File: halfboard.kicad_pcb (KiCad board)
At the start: 2 copper layers, 117.4 x 87.9 mm, 54 parts, among them U1 

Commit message: move battery/switch and correct polarity
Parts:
- removed the   at (52.6, 48.5)
- removed REF**: SW_SPDT_PCM12, Button_Switch_SMD:SW_SPDT_PCM12
- added  : , Button_Switch_SMD:SW_SPDT_PCM12, F.Cu at (135.4, 130.6)
- added  : , Button_Switch_SMD:SW_SPDT_PCM12, B.Cu at (135.4, 130.6)
-  : renamed from REF**
-  : renamed from REF**; value SW_SPST_B3U-3000P-B -> (none)
- moved   60.5 mm to (80.0, 109.2)
- moved   33.0 mm to (48.8, 47.5) (x2)
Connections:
-   pad 1: row0 -> (no net) (x6)
-   pad 2: col5_row0 -> (no net)
-   pad 2: col4_row0 -> (no net)
-   pad 2: col3_row0 -> (no net)
-   pad 1: row1 -> (no net) (x6)
-   pad 2: col3_row1 -> (no net)
-   pad 1: row2 -> (no net) (x6)
-   pad 2: col3_row2 -> (no net)
-   pad 2: col2_row2 -> (no net)
-   pad 2: col2_row1 -> (no net)
-   pad 2: col1_row2 -> (no net)
-   pad 1: row3 -> (no net) (x6)
-   pad 2: col1_row3 -> (no net)
-   pad 2: col0_row3 -> (no net)
-   pad 2: col0_row2 -> (no net)
-   pad 2: col5_row1 -> (no net)
-   pad 2: col2_row0 -> (no net)
-   pad 2: col1_row0 -> (no net)
-   pad 2: col1_row1 -> (no net)
-   pad 2: col0_row1 -> (no net)
-   pad 2: col0_row0 -> (no net)
-   pad 2: col5_row2 -> (no net)
-   pad 2: col5_row3 -> (no net)
-   pad 1: BAT0 -> BAT_SW
-   pad 2: BAT_SW -> BAT0
-   pad 2: col4_row3 -> (no net)
-   pad 2: col3_row3 -> (no net)
-   pad 2: col2_row3 -> (no net)
-   pad 2: col4_row2 -> (no net)
-   pad 2: col4_row1 -> (no net)
- U1 pad 10: col1 -> (no net)
- U1 pad 12: col3 -> col1
- U1 pad 14: col5 -> (no net)
- U1 pad 15: (no net) -> col3
- U1 pad 16: (no net) -> col5
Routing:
- net BAT_GND: track 34.4 -> 150.2 mm
- net BAT0: track 5.98 -> 60.3 mm
- net col3: track 135.2 -> 90.8 mm, vias 0 -> 1
- net BAT_SW: track 33.2 -> 74.8 mm, vias 0 -> 1
- net row2: track 165.4 -> 132.4 mm, vias 1 -> 3
- net col2: track 153.6 -> 127.7 mm, vias 0 -> 3
- net col5: track 166.3 -> 140.7 mm
- net RESET: track 13.9 -> 33.0 mm
- net col4: track 150.3 -> 131.8 mm
- net row3: track 175.1 -> 158.3 mm, vias 0 -> 2
- net row1: track 117.9 -> 131.1 mm, vias 0 -> 2
- net col1: track 78.4 -> 66.7 mm
- net col0: track 90.5 -> 80.0 mm
- net (no net): track 5.70 -> 0.00 mm
- net col0_row1: track 22.1 -> 17.0 mm
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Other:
- outline, holes or cut-outs redrawn

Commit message: remove front silkscreens
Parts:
- removed the   at (135.4, 130.6) (x2)
- added  : , Button_Switch_SMD:SW_SPDT_PCM12, F.Cu at (135.4, 130.6)
- added  : , Button_Switch_SMD:SW_SPDT_PCM12, B.Cu at (135.4, 130.6)

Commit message: update gerber files
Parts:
- removed the   at (135.4, 130.6) (x2)
- added  : , Button_Switch_SMD:SW_SPDT_PCM12, F.Cu at (135.4, 130.6)
- added  : , Button_Switch_SMD:SW_SPDT_PCM12, B.Cu at (135.4, 130.6)
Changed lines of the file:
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@@
     (add_net row3)
+  )
+  (module halfboard:ArduinoProMicro-TopSide (layer F.Cu)
+    (at 68.287231 63.5 270)
+    (fp_text reference U1 (at 0 1.625 270) (layer B.SilkS) hide
+      (effects (font (size 1.27 1.524) (thickness 0.2032)) (justify mirror))
+    )
+    (fp_text value " " (at 0 0 270) (layer F.SilkS) hide
+      (effects (font (size 1.27 1.524) (thickness 0.2032)))
+    )
+    (pad 1 thru_hole rect (at -13.97 7.62 270) (size 1.7526 1.7526) (drill 1.0922) (layers *.Cu B.SilkS))
+    (pad 2 thru_hole circle (at -11.43 7.62 270) (size 1.7526 1.7526) (drill 1.0922) (layers *.Cu *.Mask))
+    (pad 3 thru_hole circle (at -8.89 7.62 270) (size 1.7526 1.7526) (drill 1.0922) (layers *.Cu *.Mask)
+      (net 39 RESET_GND))
+    (pad 4 thru_hole circle (at -6.35 7.62 270) (size 1.7526 1.7526) (drill 1.0922) (layers *.Cu *.Mask))
+    (pad 5 thru_hole circle (at -3.81 7.62 270) (size 1.7526 1.7526) (drill 1.0922) (layers *.Cu *.Mask)
+      (net 32 row0))
+    (pad 6 thru_hole circle (at -1.27 7.62 270) (size 1.7526 1.7526) (drill 1.0922) (layers *.Cu *.Mask)
+      (net 33 row1))
+    (pad 7 thru_hole circle (at 1.27 7.62 270) (size 1.7526 1.7526) (drill 1.0922) (layers *.Cu *.Mask)
+      (net 34 row2))
+    (pad 8 thru_hole circle (at 3.81 7.62 270) (size 1.7526 1.7526) (drill 1.0922) (layers *.Cu *.Mask)
+      (net 8 row3))
+    (pad 9 thru_hole circle (at 6.35 7.62 270) (size 1.7526 1.7526) (drill 1.0922) (layers *.Cu *.Mask)
+      (net 26 col0))
+    (pad 10 thru_hole circle (at 8.89 7.62 270) (size 1.7526 1.7526) (drill 1.0922) (layers *.Cu *.Mask))
+    (pad 11 thru_hole circle (at 11.43 7.62 270) (size 1.7526 1.7526) (drill 1.0922) (layers *.Cu *.Mask)
+      (net 28 col2))
+    (pad 13 thru_hole circle (at 13.97 -7.62 270) (size 1.7526 1.7526) (drill 1.0922) (layers *.Cu *.Mask)
+      (net 30 col4))
+    (pad 14 thru_hole circle (at 11.43 -7.62 270) (size 1.7526 1.7526) (drill 1.0922) (layers *.Cu *.Mask))
+    (pad 15 thru_hole circle (at 8.89 -7.62 270) (size 1.7526 1.7526) (drill 1.0922) (layers *.Cu *.Mask)
+      (net 29 col3))
+    (pad 16 thru_hole circle (at 6.35 -7.62 270) (size 1.7526 1.7526) (drill 1.0922) (layers *.Cu *.Mask)
+      (net 31 col5))
+    (pad 17 thru_hole circle (at 3.81 -7.62 270) (size 1.7526 1.7526) (drill 1.0922) (layers *.Cu *.Mask))
+    (pad 18 thru_hole circle (at 1.27 -7.62 270) (size 1.7526 1.7526) (drill 1.0922) (layers *.Cu *.Mask))
+    (pad 19 thru_hole circle (at -1.27 -7.62 270) (size 1.7526 1.7526) (drill 1.0922) (layers *.Cu *.Mask))
+    (pad 20 thru_hole circle (at -3.81 -7.62 270) (size 1.7526 1.7526) (drill 1.0922) (layers *.Cu *.Mask))
+    (pad 21 thru_hole circle (at -6.35 -7.62 270) (size 1.7526 1.7526) (drill 1.0922) (layers *.Cu *.Mask))
+    (pad 22 thru_hole circle (at -8.89 -7.62 270) (size 1.7526 1.7526) (drill 1.0922) (layers *.Cu *.Mask)
+      (net 38 RESET))
+    (pad 23 thru_hole circle (at -11.43 -7.62 270) (size 1.7526 1.7526) (drill 1.0922) (layers *.Cu *.Mask)
+      (net 37 BAT_GND))
+    (pad 12 thru_hole circle (at 13.97 7.62 270) (size 1.7526 1.7526) (drill 1.0922) (layers *.Cu *.Mask)
+      (net 27 col1))
+    (pad 24 thru_hole circle (at -13.97 -7.62 270) (size 1.7526 1.7526) (drill 1.0922) (layers *.Cu *.Mask)
+      (net 35 BAT0))
+    (model /Users/danny/Documents/proj/custom-keyboard/kicad-libs/3d_models/Pro_Micro.wrl
+      (offset (xyz 15.23999977111816 -8.889999866485596 1.269999980926514))
+      (scale (xyz 0.395 0.395 0.395))
+      (rotate (xyz 0 0 270))
+    )
   )
   (module Button_Switch_SMD:SW_SPST_B3U-3000P-B (layer F.Cu)
@@
     (pad "" np_thru_hole circle (at 0 0 90) (size 5 5) (drill 5) (layers *.Cu *.Mask))
   )
-  (module halfboard:ArduinoProMicro-TopSide (layer F.Cu)
-    (at 68.287231 63.5 270)
-    (fp_text reference U1 (at 0 1.625 90) (layer B.SilkS) hide
-      (effects (font (size 1.27 1.524) (thickness 0.2032)) (justify mirror))
-    )
-    (fp_text value " " (at 0 0 90) (layer F.SilkS) hide
-      (effects (font (size 1.27 1.524) (thickness 0.2032)))
-    )
-    (fp_line (start -12.7 6.35) (end -12.7 8.89) (layer F.SilkS) (width 0.381))
-    (fp_line (start -15.24 6.35) (end -12.7 6.35) (layer F.SilkS) (width 0.381))
-    (pad 1 thru_hole rect (at -13.97 7.62 270) (size 1.7526 1.7526) (drill 1.0922) (layers *.Cu B.SilkS))
-    (pad 2 thru_hole circle (at -11.43 7.62 270) (size 1.7526 1.7526) (drill 1.0922) (layers *.Cu *.SilkS *.Mask))
-    (pad 3 thru_hole circle (at -8.89 7.62 270) (size 1.7526 1.7526) (drill 1.0922) (layers *.Cu *.SilkS *.Mask)
-      (net 39 RESET_GND))
-    (pad 4 thru_hole circle (at -6.35 7.62 270) (size 1.7526 1.7526) (drill 1.0922) (layers *.Cu *.SilkS *.Mask))
-    (pad 5 thru_hole circle (at -3.81 7.62 270) (size 1.7526 1.7526) (drill 1.0922) (layers *.Cu *.SilkS *.Mask)
-      (net 32 row0))
-    (pad 6 thru_hole circle (at -1.27 7.62 270) (size 1.7526 1.7526) (drill 1.0922) (layers *.Cu *.SilkS *.Mask)
-      (net 33 row1))
-    (pad 7 thru_hole circle (at 1.27 7.62 270) (size 1.7526 1.7526) (drill 1.0922) (layers *.Cu *.SilkS *.Mask)
-      (net 34 row2))
-    (pad 8 thru_hole circle (at 3.81 7.62 270) (size 1.7526 1.7526) (drill 1.0922) (layers *.Cu *.SilkS *.Mask)
-      (net 8 row3))
-    (pad 9 thru_hole circle (at 6.35 7.62 270) (size 1.7526 1.7526) (drill 1.0922) (layers *.Cu *.SilkS *.Mask)
-      (net 26 col0))
-    (pad 10 thru_hole circle (at 8.89 7.62 270) (size 1.7526 1.7526) (drill 1.0922) (layers *.Cu *.SilkS *.Mask))
-    (pad 11 thru_hole circle (at 11.43 7.62 270) (size 1.7526 1.7526) (drill 1.0922) (layers *.Cu *.SilkS *.Mask)
-      (net 28 col2))
-    (pad 13 thru_hole circle (at 13.97 -7.62 270) (size 1.7526 1.7526) (drill 1.0922) (layers *.Cu *.SilkS *.Mask)
-      (net 30 col4))
-    (pad 14 thru_hole circle (at 11.43 -7.62 270) (size 1.7526 1.7526) (drill 1.0922) (layers *.Cu *.SilkS *.Mask))
-    (pad 15 thru_hole circle (at 8.89 -7.62 270) (size 1.7526 1.7526) (drill 1.0922) (layers *.Cu *.SilkS *.Mask)
-      (net 29 col3))
-    (pad 16 thru_hole circle (at 6.35 -7.62 270) (size 1.7526 1.7526) (drill 1.0922) (layers *.Cu *.SilkS *.Mask)
-      (net 31 col5))
-    (pad 17 thru_hole circle (at 3.81 -7.62 270) (size 1.7526 1.7526) (drill 1.0922) (layers *.Cu *.SilkS *.Mask))
-    (pad 18 thru_hole circle (at 1.27 -7.62 270) (size 1.7526 1.7526) (drill 1.0922) (layers *.Cu *.SilkS *.Mask))
-    (pad 19 thru_hole circle (at -1.27 -7.62 270) (size 1.7526 1.7526) (drill 1.0922) (layers *.Cu *.SilkS *.Mask))
-    (pad 20 thru_hole circle (at -3.81 -7.62 270) (size 1.7526 1.7526) (drill 1.0922) (layers *.Cu *.SilkS *.Mask))
-    (pad 21 thru_hole circle (at -6.35 -7.62 270) (size 1.7526 1.7526) (drill 1.0922) (layers *.Cu *.SilkS *.Mask))
-    (pad 22 thru_hole circle (at -8.89 -7.62 270) (size 1.7526 1.7526) (drill 1.0922) (layers *.Cu *.SilkS *.Mask)
-      (net 38 RESET))
-    (pad 23 thru_hole circle (at -11.43 -7.62 270) (size 1.7526 1.7526) (drill 1.0922) (layers *.Cu *.SilkS *.Mask)
-      (net 37 BAT_GND))
-    (pad 12 thru_hole circle (at 13.97 7.62 270) (size 1.7526 1.7526) (drill 1.0922) (layers *.Cu *.SilkS *.Mask)
-      (net 27 col1))
-    (pad 24 thru_hole circle (at -13.97 -7.62 270) (size 1.7526 1.7526) (drill 1.0922) (layers *.Cu *.SilkS *.Mask)
-      (net 35 BAT0))
-    (model /Users/danny/Documents/proj/custom-keyboard/kicad-libs/3d_models/Pro_Micro.wrl
-      (offset (xyz 15.23999977111816 -8.889999866485596 1.269999980926514))
-      (scale (xyz 0.395 0.395 0.395))
-      (rotate (xyz 0 0 270))
-    )
-  )
   (module Button_Switch_SMD:SW_SPDT_PCM12 (layer B.Cu)

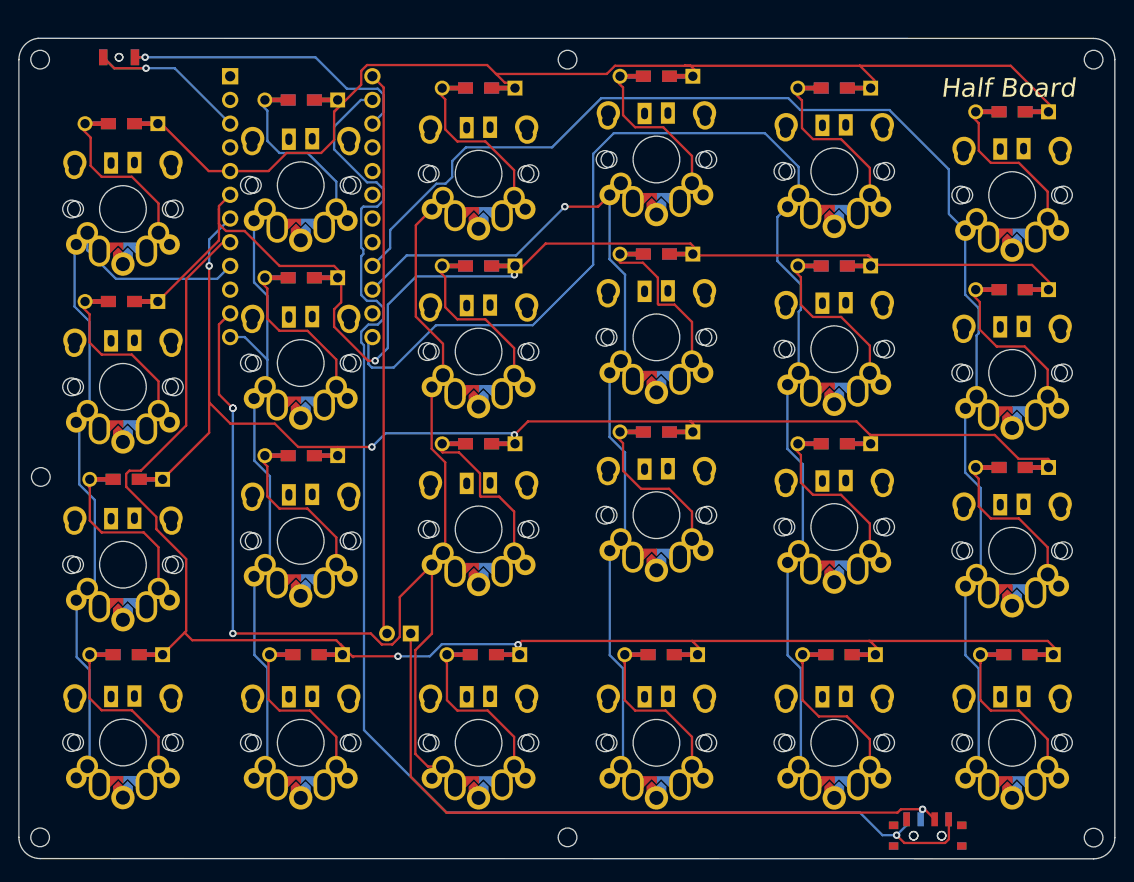
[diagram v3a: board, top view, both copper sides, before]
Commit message: update layout and remove more silkscreen
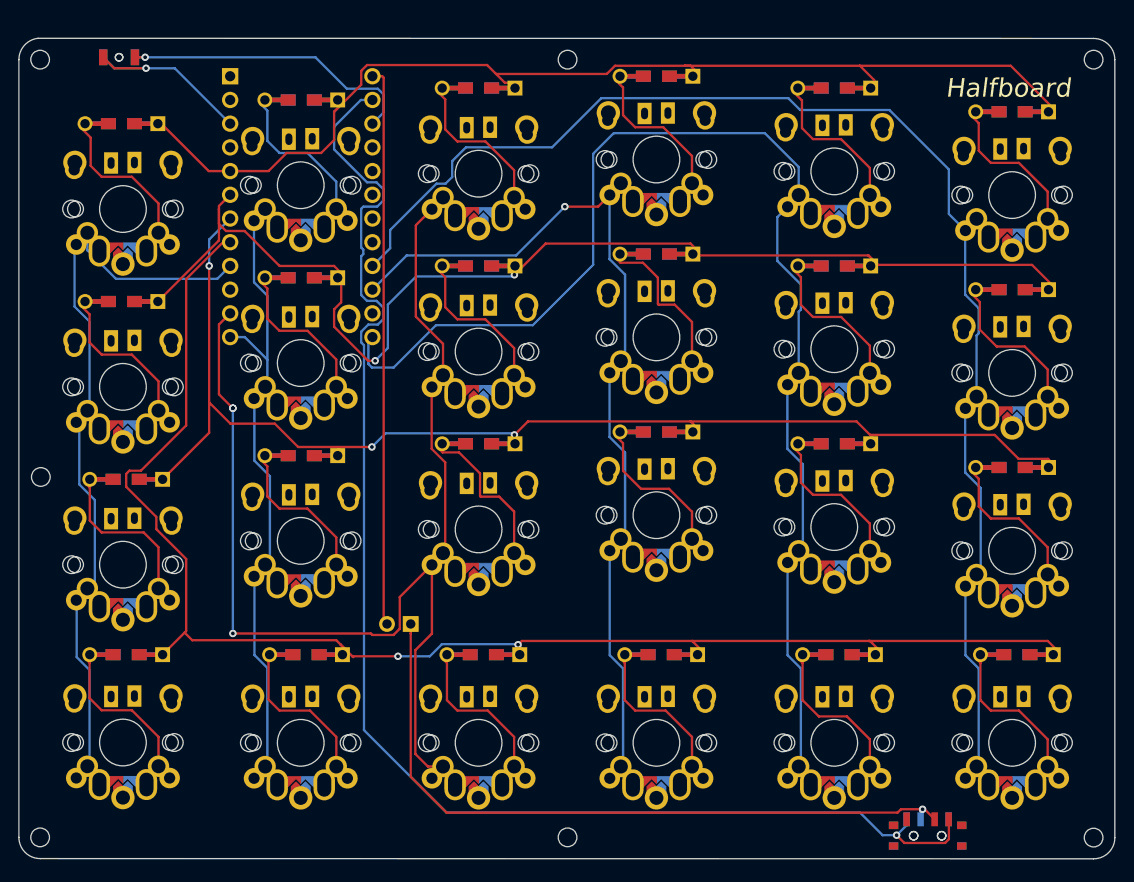
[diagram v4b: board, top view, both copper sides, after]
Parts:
- removed the   at (135.4, 130.6) (x2)
- added  : , Button_Switch_SMD:SW_SPDT_PCM12, F.Cu at (135.4, 130.6)
- added  : , Button_Switch_SMD:SW_SPDT_PCM12, B.Cu at (135.4, 130.6)
- moved   1.02 mm to (80.0, 108.2)
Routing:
- net col2: track 127.7 -> 126.4 mm
- net BAT_SW: track 74.8 -> 75.8 mm
- net BAT0: track 60.3 -> 59.8 mm
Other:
- board text added: "Halfboard"
- board text removed: "Half Board"
